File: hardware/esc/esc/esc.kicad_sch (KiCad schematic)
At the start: 9 parts, among them IC1 XMC1100T016F0016ABXUMA1, IC2 STDRIVE101TR, Q1 BSC030P03NS3G, Q2 BSC030P03NS3G, Q3 BSC030P03NS3G, Q4 BSC030P03NS3G, Q5 BSC030P03NS3G, Q6 BSC030P03NS3G, U1 AP62300Z6

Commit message: hardware edits mainly
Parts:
- removed IC1: XMC1100T016F0016ABXUMA1, SOP65P640X120-16N, symbol XMC1100T016F0016ABXUMA1:XMC1100T016F0016ABXUMA1
- removed IC2: STDRIVE101TR, QFN50P400X400X100-25N-D, symbol STDRIVE101TR:STDRIVE101TR
- removed Q1, Q2, Q3, Q4, Q5, Q6: BSC030P03NS3G, BSC0902NSATMA1, symbol BSC030N03LSGATMA1:BSC030P03NS3G
- removed U1: AP62300Z6, Package_TO_SOT_SMD:SOT-563, symbol Regulator_Switching:AP62300Z6
- added C1, C10, C11, C16, C17, C18, C23, C24, C25, C3, C30, C31, C32, C39, C40, C41, C43, C44, C45, C46, C48, C5, C50, C51, C54, C55, C57, C58, C60, C61, C63, C64, C66, C67, C71, C72, C73, C74, C75, C76, C84, C85, C88, C9, C91: 4.7uF, Capacitor_SMD:CP_Elec_6.3x7.7, symbol Device:C_Small
- added C12, C13, C14, C19, C2, C20, C21, C26, C27, C28, C33, C34, C35, C36, C37, C38, C4, C52, C53, C56, C59, C6, C62, C65, C83, C86, C89, C92: 220nF, Capacitor_SMD:C_0402_1005Metric, symbol Device:C_Small
- added C15, C22, C29, C42, C7, C8: 1nF, Capacitor_SMD:C_0603_1608Metric, symbol Device:C_Small
- added C47, C49: 18pF, Capacitor_SMD:C_0402_1005Metric, symbol Device:C_Small
- added C68: 1uF, Capacitor_SMD:C_0603_1608Metric, symbol Device:C_Small
- added C69, C70, C77, C78, C79, C80, C81, C82, C87, C90, C93: 0.1uF, Capacitor_SMD:C_0603_1608Metric, symbol Device:C_Small
- added D1, D10, D11, D12, D13, D14, D15, D16, D17, D18, D19, D2, D3, D4, D5, D6, D7, D8, D9: D_Small, Diode_SMD:D_SMA, symbol Device:D_Small
- added IC1, IC2, IC3, IC4, IC5, IC6: IR2136SPBF, SOIC127P1032X265-28N, symbol IR2136SPBF:IR2136SPBF
- added IC7: TLA2528IRTER, Package_DFN_QFN:WQFN-16-1EP_3x3mm_P0.5mm_EP1.68x1.68mm_ThermalVias, symbol TLA2528IRTER:TLA2528IRTER
- added IC8: MP9486AGN-Z, Package_SO:SOIC-8-1EP_3.9x4.9mm_P1.27mm_EP2.62x3.51mm_ThermalVias, symbol MP9486AGN-Z:MP9486AGN-Z
- added J1: USB-C, Connector_PinHeader_2.54mm:PinHeader_1x04_P2.54mm_Vertical, symbol Connector:Conn_01x04_Pin
- added J10: GPIO, Connector_PinHeader_2.54mm:PinHeader_1x04_P2.54mm_Vertical, symbol Connector:Conn_01x04_Pin
- added J11: Conn_01x08_Pin, Connector_PinHeader_1.27mm:PinHeader_1x08_P1.27mm_Vertical, symbol Connector:Conn_01x08_Pin
- added J2: DEBUG, Connector_PinHeader_2.54mm:PinHeader_1x04_P2.54mm_Vertical, symbol Connector:Conn_01x04_Pin
- added J3: TEMP-GPIO, Connector_PinHeader_1.27mm:PinHeader_1x08_P1.27mm_Vertical, symbol Connector:Conn_01x08_Pin
- added L1: 3.3uH, Inductor_SMD:L_0805_2012Metric_Pad1.05x1.20mm_HandSolder, symbol Device:L_Small
- added L2: 33uH, Inductor_SMD:L_0805_2012Metric, symbol Device:L_Small
- added Q1, Q10, Q11, Q12, Q13, Q14, Q15, Q16, Q17, Q18, Q19, Q2, Q20, Q21, Q22, Q23, Q24, Q25, Q26, Q27, Q28, Q29, Q3, Q30, Q31, Q32, Q33, Q34, Q35, Q36, Q4, Q5, Q6, Q7, Q8, Q9: NMOS, Package_SO:PowerPAK_SO-8L_Single, symbol Simulation_SPICE:NMOS
- added R1, R2, R22, R23, R24, R25, R26, R27, R3, R34, R35, R36, R37, R38, R39, R4, R46, R47, R48, R49, R5, R50, R51, R58, R59, R6, R60, R61, R62, R63, R79, R80, R81, R82, R83, R84: 10, Resistor_SMD:R_1206_3216Metric, symbol Device:R_Small
- added R10, R11, R12, R13, R14, R15, R19, R20, R21, R31, R32, R33, R43, R44, R45, R55, R56, R57, R64, R65, R66, R67, R68, R69, R70, R71, R72, R73, R74, R75, R76, R77, R78: SHUNT, Fuse:Fuse_1206_3216Metric_Pad1.42x1.75mm_HandSolder, symbol Device:R_Small
- added R16, R17, R18, R28, R29, R30, R40, R41, R42, R52, R53, R54, R7, R8, R88, R89, R9, R90: 4.7, Resistor_SMD:R_0805_2012Metric, symbol Device:R_Small
- added R91, R92: 27, Resistor_SMD:R_0402_1005Metric, symbol Device:R_Small
- added R93, R94: 1k, Resistor_SMD:R_0201_0603Metric, symbol Device:R_Small
- added R95: 33, Resistor_SMD:R_1206_3216Metric, symbol Device:R_Small
- added R96: 240k, Resistor_SMD:R_0402_1005Metric, symbol Device:R_Small
- added R97, R98: 10k, Resistor_SMD:R_0402_1005Metric, symbol Device:R_Small
- added SW1, SW2: SW_Push, Connector_PinHeader_2.54mm:PinHeader_1x02_P2.54mm_Vertical, symbol Switch:SW_Push
- added TP1, TP10, TP11, TP12, TP13, TP14, TP15, TP16, TP17, TP18, TP2, TP3, TP4, TP5, TP6, TP7, TP8, TP9: TestPoint_Small, TestPoint:TestPoint_Pad_4.0x4.0mm, symbol Connector:TestPoint_Small
- added TP19, TP20, TP21, TP22: TestPoint, TestPoint:TestPoint_Pad_4.0x4.0mm, symbol Connector:TestPoint
- added U1: RP2354B, Package_DFN_QFN:QFN-80-1EP_10x10mm_P0.4mm_EP3.4x3.4mm, symbol MCU_RaspberryPi:RP2354B
- added U10, U11, U12, U2, U3, U4, U5, U6, U7, U8, U9: INA240A2PW, Package_SO:TSSOP-8_4.4x3mm_P0.65mm, symbol Amplifier_Current:INA240A2PW
- added U14, U15: TMP110D, Package_SON:Texas_X2SON-5_0.8x0.8mm_P0.48mm, symbol Sensor_Temperature:TMP110D
- added U16: AZ1117CH2-3.3, Package_TO_SOT_SMD:SOT-223-3_TabPin2, symbol Regulator_Linear:AZ1117CH2-3.3
- added Y1: 12MHz, Crystal:Crystal_SMD_ECS_CSM3X-2Pin_7.6x4.1mm, symbol Device:Crystal
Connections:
- new net: C49.2, U1.30 (XIN), Y1.2
- new net: C16.1, C19.1, IC3.22 (VS2), Q15.1 (S), Q15.2 (S), Q15.3 (S), Q16.5 (D), TP8.1
- new net: C16.2, C19.2, IC3.24 (VB2), R29.1
- new net: Q10.1 (S), Q10.2 (S), Q10.3 (S), Q12.1 (S), Q12.2 (S), Q12.3 (S), Q8.1 (S), Q8.2 (S), Q8.3 (S), R19.2, R20.2, R21.2, U4.2 (+)
- new net: J1.2 (Pin_2), R91.2
- new net: J1.3 (Pin_3), R92.1
- new net: C11.2, C14.2, IC2.20 (VB3), R18.1
- new net: D5.1 (K), R18.2
- new net: Q4.1 (S), Q4.2 (S), Q4.3 (S), Q5.1 (S), Q5.2 (S), Q5.3 (S), Q6.1 (S), Q6.2 (S), Q6.3 (S), R10.2, R11.2, R12.2, U2.2 (+)
- new net: Q4.4 (G), R4.2
- new net: C5.2, C6.1, IC1.18 (VS3), Q1.1 (S), Q1.2 (S), Q1.3 (S), Q4.5 (D), TP6.1
- new net: C30.1, C33.1, IC5.22 (VS2), Q27.1 (S), Q27.2 (S), Q27.3 (S), Q28.5 (D), TP18.1
- new net: C30.2, C33.2, IC5.24 (VB2), R53.1
- new net: C32.2, C35.2, IC5.20 (VB3), R54.1
- new net: D14.1 (K), R54.2
- new net: C17.1, C20.1, IC3.28 (VB1), R28.1
- new net: C17.2, C20.2, IC3.26 (VS1), Q17.1 (S), Q17.2 (S), Q17.3 (S), Q18.5 (D), TP7.1
- new net: Q35.1 (S), Q35.2 (S), Q35.3 (S), R76.2, R77.2, R78.2, U12.2 (+)
- new net: Q35.4 (G), R84.2
- new net: C36.1, C39.1, IC6.18 (VS3), Q35.5 (D), Q36.1 (S), Q36.2 (S), Q36.3 (S), TP15.1
- new net: IC1.23 (HO2), R2.1
- new net: Q2.4 (G), R2.2
- new net: IC2.15 (LO2), R24.1
- new net: Q10.4 (G), R24.2
- new net: Q28.1 (S), Q28.2 (S), Q28.3 (S), R67.2, R68.2, R69.2, U8.2 (+)
- new net: Q28.4 (G), R60.2
- new net: Q20.1 (S), Q20.2 (S), Q20.3 (S), Q22.1 (S), Q22.2 (S), Q22.3 (S), Q24.1 (S), Q24.2 (S), Q24.3 (S), R43.2, R44.2, R45.2, U6.2 (+)
- new net: C47.2, U1.31 (XOUT), Y1.1
- new net: C29.1, IC5.11 (RCIN)
- new net: R93.2, SW1.1, SW2.1, U1.35 (RUN)
- new net: R94.1, SW2.2
- new net: Q36.4 (G), R83.2
- new net: IC2.23 (HO2), R26.1
- new net: Q9.4 (G), R26.2
- new net: D15.1 (K), R53.2
- new net: C22.1, IC4.11 (RCIN)
- new net: C23.1, C26.1, IC4.22 (VS2), Q21.1 (S), Q21.2 (S), Q21.3 (S), Q22.5 (D), TP11.1
- new net: C23.2, C26.2, IC4.24 (VB2), R41.1
- new net: Q17.4 (G), R39.2
- new net: C31.1, C34.1, IC5.28 (VB1), R52.1
- new net: C31.2, C34.2, IC5.26 (VS1), Q29.1 (S), Q29.2 (S), Q29.3 (S), Q30.5 (D), TP17.1
- new net: C10.2, C13.2, IC2.26 (VS1), Q11.1 (S), Q11.2 (S), Q11.3 (S), Q12.5 (D), TP1.1
- new net: Q31.1 (S), Q31.2 (S), Q31.3 (S), R13.2, R14.2, R15.2, U10.2 (+)
- new net: C25.1, C28.1, IC4.18 (VS3), Q19.1 (S), Q19.2 (S), Q19.3 (S), Q20.5 (D), TP12.1
- new net: Q19.4 (G), R47.2
- new net: IC3.27 (HO1), R39.1
- new net: C12.2, C9.1, IC2.24 (VB2), R17.1
- new net: D6.1 (K), R17.2
- new net: IC5.19 (HO3), R59.1
- new net: Q25.4 (G), R59.2
- new net: Q14.1 (S), Q14.2 (S), Q14.3 (S), Q16.1 (S), Q16.2 (S), Q16.3 (S), Q18.1 (S), Q18.2 (S), Q18.3 (S), R31.2, R32.2, R33.2, U5.2 (+)
- new net: Q18.4 (G), R37.2
- new net: IC7.13 (SCL), U1.12 (GPIO13), U14.2 (SCL), U15.2 (SCL)
- new net: U1.13 (GPIO14), U14.3 (ADD0)
- new net: IC7.14 (SDA), U1.11 (GPIO12), U14.4 (SDA), U15.4 (SDA)
- new net: Q5.4 (G), R5.2
- new net: C3.2, C4.1, IC1.22 (VS2), Q2.1 (S), Q2.2 (S), Q2.3 (S), Q5.5 (D), TP5.1
- new net: C24.2, C27.2, IC4.26 (VS1), Q23.1 (S), Q23.2 (S), Q23.3 (S), Q24.5 (D), TP10.1
- new net: C25.2, C28.2, IC4.20 (VB3), R42.1
- new net: D11.1 (K), R42.2
- new net: C18.1, C21.1, IC3.18 (VS3), Q13.1 (S), Q13.2 (S), Q13.3 (S), Q14.5 (D), TP9.1
- new net: C18.2, C21.2, IC3.20 (VB3), R30.1
- new net: C36.2, C39.2, IC6.20 (VB3), R88.1
- new net: C37.2, C40.2, IC6.26 (VS1), Q31.5 (D), Q32.1 (S), Q32.2 (S), Q32.3 (S), TP13.1
- new net: D9.1 (K), R29.2
- new net: D3.1 (K), R9.2
- new net: Q8.4 (G), R22.2
- new net: C11.1, C14.1, IC2.18 (VS3), Q7.1 (S), Q7.2 (S), Q7.3 (S), Q8.5 (D), TP3.1
- new net: Q33.1 (S), Q33.2 (S), Q33.3 (S), R73.2, R74.2, R75.2, U11.2 (+)
- new net: R55.2, R56.2, R57.2, R64.1, R65.1, R66.1, R67.1, R68.1, R69.1, R70.1, R71.1, R72.1, U7.2 (+)
- new net: Q30.1 (S), Q30.2 (S), Q30.3 (S), R64.2, R65.2, R66.2, U3.2 (+)
- new net: Q6.4 (G), R6.2
- new net: C1.2, C2.2, IC1.26 (VS1), Q3.1 (S), Q3.2 (S), Q3.3 (S), Q6.5 (D), TP4.1
- new net: C1.1, C2.1, IC1.28 (VB1), R8.1
- new net: R93.1, U1.75 (~{QSPI_SS})
- new net: Q29.4 (G), R63.2
- new net: D18.1 (K), R90.2
- new net: C38.1, C41.1, IC6.22 (VS2), Q33.5 (D), Q34.1 (S), Q34.2 (S), Q34.3 (S), TP14.1
- new net: Q34.4 (G), R80.2
- new net: IC8.6 (DIM), IC8.7 (EN), R98.1
- new net: Q26.1 (S), Q26.2 (S), Q26.3 (S), R70.2, R71.2, R72.2, U9.2 (+)
- new net: IC4.23 (HO2), R50.1
- new net: Q21.4 (G), R50.2
- new net: C38.2, C41.2, IC6.24 (VB2), R89.1
- new net: C42.1, IC6.11 (RCIN)
- new net: Q22.4 (G), R48.2
- new net: IC6.15 (LO2), R82.1
- new net: Q33.4 (G), R82.2
- new net: D1.1 (K), R8.2
- new net: D12.1 (K), R41.2
- new net: C44.1, R95.1, U1.61 (VREG_AVDD)
- new net: IC5.14 (LO3), R61.1
- new net: Q30.4 (G), R61.2
- new net: IC4.16 (LO1), R46.1
- new net: Q20.4 (G), R46.2
- new net: Q26.4 (G), R58.2
- new net: C32.1, C35.1, IC5.18 (VS3), Q25.1 (S), Q25.2 (S), Q25.3 (S), Q26.5 (D), TP16.1
- new net: C77.1, U16.2 (GND)
- new net: IC4.15 (LO2), R48.1
- new net: IC7.15 (AIN0/GPIO0), J3.1 (Pin_1)
- new net: IC7.16 (AIN1/GPIO1), J3.2 (Pin_2)
- new net: IC7.1 (AIN2/GPIO2), J3.3 (Pin_3)
- new net: IC7.2 (AIN3/GPIO3), J3.4 (Pin_4)
- new net: IC7.3 (AIN4/GPIO4), J3.5 (Pin_5)
- new net: IC7.4 (AIN5/GPIO5), J3.6 (Pin_6)
- new net: IC7.5 (AIN6/GPIO6), J3.7 (Pin_7)
- new net: IC7.6 (AIN7/GPIO7), J3.8 (Pin_8)
- new net: IC2.14 (LO3), R25.1
- new net: Q12.4 (G), R25.2
- new net: IC1.9 (ITRIP), U1.4 (GPIO7), U2.8
- new net: U1.54 (GPIO43/ADC3), U10.8
- new net: Q31.4 (G), R81.2
- new net: D4.1 (K), R16.2
- new net: C10.1, C13.1, IC2.28 (VB1), R16.1
- new net: IC3.10 (EN), U1.44 (GPIO35)
- new net: C15.1, IC3.11 (RCIN)
- new net: IC3.14 (LO3), R37.1
- new net: IC3.15 (LO2), R36.1
- new net: IC3.16 (LO1), R34.1
- new net: IC3.19 (HO3), R35.1
- new net: IC3.2 (~{HIN1}), IC4.2 (~{HIN1}), IC5.2 (~{HIN1}), U1.38 (GPIO30)
- new net: IC3.23 (HO2), R38.1
- new net: IC3.3 (~{HIN2}), IC4.3 (~{HIN2}), IC5.3 (~{HIN2}), U1.40 (GPIO32)
- new net: IC3.4 (~{HIN3}), IC4.4 (~{HIN3}), IC5.4 (~{HIN3}), U1.43 (GPIO34)
- new net: IC3.5 (~{LIN1}), IC4.5 (~{LIN1}), IC5.5 (~{LIN1}), U1.45 (GPIO36)
- new net: IC3.6 (~{LIN2}), IC4.6 (~{LIN2}), IC5.6 (~{LIN2}), U1.47 (GPIO38)
- new net: IC3.7 (~{LIN3}), IC4.7 (~{LIN3}), IC5.7 (~{LIN3}), U1.48 (GPIO39)
- new net: IC3.8 (~{FAULT}), U1.46 (GPIO37)
- new net: IC3.9 (ITRIP), U1.26 (GPIO25), U5.8
- new net: IC1.14 (LO3), R6.1
- new net: C70.2, IC8.1 (FB), R96.1, R97.2
- new net: Q1.4 (G), R3.2
- new net: C24.1, C27.1, IC4.28 (VB1), R40.1
- new net: Q14.4 (G), R34.2
- new net: C37.1, C40.1, IC6.28 (VB1), R90.1
- new net: D13.1 (K), R52.2
- new net: Q32.4 (G), R79.2
- new net: C68.1, IC7.8 (DECAP)
- new net: IC6.23 (HO2), R80.1
- new net: Q3.4 (G), R1.2
- new net: IC2.10 (EN), U1.9 (GPIO11)
- new net: C8.1, IC2.11 (RCIN)
- new net: IC2.16 (LO1), R22.1
- new net: IC2.19 (HO3), R23.1
- new net: IC1.2 (~{HIN1}), IC2.2 (~{HIN1}), IC6.2 (~{HIN1}), U1.77 (GPIO0)
- new net: C12.1, C9.2, IC2.22 (VS2), Q10.5 (D), Q9.1 (S), Q9.2 (S), Q9.3 (S), TP2.1
- new net: IC2.27 (HO1), R27.1
- new net: IC1.3 (~{HIN2}), IC2.3 (~{HIN2}), IC6.3 (~{HIN2}), U1.79 (GPIO2)
- new net: IC1.4 (~{HIN3}), IC2.4 (~{HIN3}), IC6.4 (~{HIN3}), U1.1 (GPIO4)
- new net: IC1.5 (~{LIN1}), IC2.5 (~{LIN1}), IC6.5 (~{LIN1}), U1.3 (GPIO6)
- new net: IC1.6 (~{LIN2}), IC2.6 (~{LIN2}), IC6.6 (~{LIN2}), U1.6 (GPIO8)
- new net: IC1.7 (~{LIN3}), IC2.7 (~{LIN3}), IC6.7 (~{LIN3}), U1.8 (GPIO10)
- new net: IC2.8 (~{FAULT}), U1.7 (GPIO9)
- new net: IC2.9 (ITRIP), U1.58 (GPIO47/ADC7), U4.8
- new net: D16.1 (K), R89.2
- new net: L1.2, U1.63 (VREG_LX)
- new net: C5.1, C6.2, IC1.20 (VB3), R9.1
- new net: IC4.14 (LO3), R49.1
- new net: Q24.4 (G), R49.2
- new net: IC1.15 (LO2), R5.1
- new net: D17.1 (K), R88.2
- new net: U1.14 (GPIO15), U15.3 (ADD0)
- new net: IC7.11 (ADDR), U1.2 (GPIO5)
- new net: C69.1, D19.1 (K), IC8.5 (SW), L2.2
- new net: C69.2, IC8.4 (BST)
- new net: C3.1, C4.2, IC1.24 (VB2), R7.1
- new net: IC1.19 (HO3), R3.1
- new net: D2.1 (K), R7.2
- new net: IC6.16 (LO1), R84.1
- new net: D10.1 (K), R40.2
- new net: U1.56 (GPIO45/ADC5), U12.8
- new net: Q27.4 (G), R62.2
- new net: IC5.9 (ITRIP), U7.8
- new net: IC6.27 (HO1), R79.1
- new net: IC1.16 (LO1), R4.1
- new net: IC4.27 (HO1), R51.1
- new net: Q23.4 (G), R51.2
- new net: Q16.4 (G), R36.2
- new net: U1.53 (GPIO42/ADC2), U9.8
- new net: Q13.4 (G), R35.2
- new net: IC1.27 (HO1), R1.1
- new net: Q11.4 (G), R27.2
- new net: IC5.27 (HO1), R63.1
- new net: R92.2, U1.67 (USB_DP)
- new net: J11.3 (Pin_3), U1.25 (GPIO24)
- new net: J11.4 (Pin_4), U1.23 (GPIO23)
- new net: J11.5 (Pin_5), U1.22 (GPIO22)
- new net: J11.6 (Pin_6), U1.21 (GPIO21)
- new net: IC4.9 (ITRIP), U1.57 (GPIO46/ADC6), U6.8
- new net: J2.3 (Pin_3), U1.33 (SWCLK)
- new net: J2.4 (Pin_4), U1.34 (SWDIO)
- new net: J10.1 (Pin_1), U1.19 (GPIO19)
- new net: J10.2 (Pin_2), U1.18 (GPIO18)
- new net: J10.3 (Pin_3), U1.17 (GPIO17)
- new net: J10.4 (Pin_4), U1.16 (GPIO16)
- new net: IC4.19 (HO3), R47.1
- new net: IC1.10 (EN), U1.80 (GPIO3)
- new net: C7.1, IC1.11 (RCIN)
- new net: IC1.8 (~{FAULT}), U1.78 (GPIO1)
- new net: IC5.10 (EN), U1.36 (GPIO28)
- new net: IC5.15 (LO2), R60.1
- new net: IC5.16 (LO1), R58.1
- new net: IC5.23 (HO2), R62.1
- new net: IC5.8 (~{FAULT}), U1.37 (GPIO29)
- new net: D7.1 (K), R28.2
- new net: D8.1 (K), R30.2
- new net: Q15.4 (G), R38.2
- new net: R91.1, U1.66 (USB_DM)
- new net: IC4.10 (EN), U1.39 (GPIO31)
- new net: IC4.8 (~{FAULT}), U1.42 (GPIO33)
- new net: IC6.8 (~{FAULT}), U1.27 (GPIO26)
- new net: IC6.10 (EN), U1.28 (GPIO27)
- new net: U1.49 (GPIO40/ADC0), U3.8
- new net: U1.52 (GPIO41/ADC1), U8.8
- new net: U1.55 (GPIO44/ADC4), U11.8
- new net: Q7.4 (G), R23.2
- new net: IC6.14 (LO3), R81.1
- new net: IC6.19 (HO3), R83.1
- new net +1V1: C43.2, C46.2, J2.1 (Pin_1), L1.1, U1.10 (DVDD), U1.32 (DVDD), U1.51 (DVDD), U1.65 (VREG_FB)
- new net +3V3: C45.1, C48.2, C50.1, C51.1, C52.1, C53.1, C54.1, C55.1, C56.1, C57.1, C58.1, C59.1, C60.1, C61.1, C62.1, C63.1, C64.1, C65.1, C66.1, C67.1, C77.2, C78.2, C79.2, C80.2, C81.2, D1.2 (A), D10.2 (A), D11.2 (A), D12.2 (A), D13.2 (A), D14.2 (A), D15.2 (A), D16.2 (A), D17.2 (A), D18.2 (A), D2.2 (A), D3.2 (A), D4.2 (A), D5.2 (A), D6.2 (A), D7.2 (A), D8.2 (A), D9.2 (A), IC1.1 (VCC), IC2.1 (VCC), IC3.1 (VCC), IC4.1 (VCC), IC5.1 (VCC), IC6.1 (VCC), IC7.10 (DVDD), IC7.7 (AVDD), J2.2 (Pin_2), R95.2, U1.15 (IOVDD), U1.24 (IOVDD), U1.29 (IOVDD), U1.41 (IOVDD), U1.5 (IOVDD), U1.50 (IOVDD), U1.59 (ADC_AVDD), U1.60 (IOVDD), U1.64 (VREG_VIN), U1.69 (QSPI_IOVDD), U1.76 (IOVDD), U10.5 (V+), U10.6 (REF2), U11.5 (V+), U11.6 (REF2), U12.5 (V+), U12.6 (REF2), U14.5 (V+), U15.5 (V+), U16.3 (OUT), U2.5 (V+), U2.6 (REF2), U3.5 (V+), U3.6 (REF2), U4.5 (V+), U4.6 (REF2), U5.5 (V+), U5.6 (REF2), U6.5 (V+), U6.6 (REF2), U7.5 (V+), U7.6 (REF2), U8.5 (V+), U8.6 (REF2), U9.5 (V+), U9.6 (REF2)
- new net +5V: C70.1, C71.1, C72.1, C73.1, C74.1, C75.1, C76.1, C82.2, C83.1, C84.1, C85.1, C86.1, C87.2, C88.2, C89.2, C90.1, C91.2, C92.2, C93.1, J1.4 (Pin_4), J11.2 (Pin_2), L2.1, R96.2, U16.1 (IN)
- new net +BATT: IC8.3 (VIN), J11.7 (Pin_7), Q1.5 (D), Q11.5 (D), Q13.5 (D), Q15.5 (D), Q17.5 (D), Q19.5 (D), Q2.5 (D), Q21.5 (D), Q23.5 (D), Q25.5 (D), Q27.5 (D), Q29.5 (D), Q3.5 (D), Q32.5 (D), Q34.5 (D), Q36.5 (D), Q7.5 (D), Q9.5 (D), R98.2, TP20.1, TP21.1
- new net GND: C15.2, C22.2, C29.2, C42.2, C43.1, C44.2, C45.2, C46.1, C47.1, C48.1, C49.1, C50.2, C51.2, C52.2, C53.2, C54.2, C55.2, C56.2, C57.2, C58.2, C59.2, C60.2, C61.2, C62.2, C63.2, C64.2, C65.2, C66.2, C67.2, C68.2, C7.2, C71.2, C72.2, C73.2, C74.2, C75.2, C76.2, C78.1, C79.1, C8.2, C80.1, C81.1, C82.1, C83.2, C84.2, C85.2, C86.2, C87.1, C88.1, C89.1, C90.2, C91.1, C92.1, C93.2, D19.2 (A), IC1.12 (VSS), IC1.13 (COM), IC1.17 (NC_1), IC1.21 (NC_2), IC1.25 (NC_3), IC2.12 (VSS), IC2.13 (COM), IC2.17 (NC_1), IC2.21 (NC_2), IC2.25 (NC_3), IC3.12 (VSS), IC3.13 (COM), IC3.17 (NC_1), IC3.21 (NC_2), IC3.25 (NC_3), IC4.12 (VSS), IC4.13 (COM), IC4.17 (NC_1), IC4.21 (NC_2), IC4.25 (NC_3), IC5.12 (VSS), IC5.13 (COM), IC5.17 (NC_1), IC5.21 (NC_2), IC5.25 (NC_3), IC6.12 (VSS), IC6.13 (COM), IC6.17 (NC_1), IC6.21 (NC_2), IC6.25 (NC_3), IC7.17 (EP), IC7.9 (GND), IC8.8 (GND), IC8.9 (EP), J1.1 (Pin_1), J11.1 (Pin_1), J11.8 (Pin_8), R10.1, R11.1, R12.1, R13.1, R14.1, R15.1, R19.1, R20.1, R21.1, R31.1, R32.1, R33.1, R43.1, R44.1, R45.1, R55.1, R56.1, R57.1, R73.1, R74.1, R75.1, R76.1, R77.1, R78.1, R94.2, R97.1, SW1.2, TP19.1, TP22.1, U1.62 (VREG_PGND), U1.81 (GND), U10.1 (GND), U10.3 (-), U10.4 (GND), U10.7 (REF1), U11.1 (GND), U11.3 (-), U11.4 (GND), U11.7 (REF1), U12.1 (GND), U12.3 (-), U12.4 (GND), U12.7 (REF1), U14.1 (GND), U15.1 (GND), U2.1 (GND), U2.3 (-), U2.4 (GND), U2.7 (REF1), U3.1 (GND), U3.3 (-), U3.4 (GND), U3.7 (REF1), U4.1 (GND), U4.3 (-), U4.4 (GND), U4.7 (REF1), U5.1 (GND), U5.3 (-), U5.4 (GND), U5.7 (REF1), U6.1 (GND), U6.3 (-), U6.4 (GND), U6.7 (REF1), U7.1 (GND), U7.3 (-), U7.4 (GND), U7.7 (REF1), U8.1 (GND), U8.3 (-), U8.4 (GND), U8.7 (REF1), U9.1 (GND), U9.3 (-), U9.4 (GND), U9.7 (REF1)

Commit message: block 1x1
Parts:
- removed R55, R56, R57: SHUNT, Fuse:Fuse_1206_3216Metric_Pad1.42x1.75mm_HandSolder, symbol Device:R_Small
- removed U7: INA240A2PW, Package_SO:TSSOP-8_4.4x3mm_P0.65mm, symbol Amplifier_Current:INA240A2PW
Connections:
- net GND: now also R64.1, R65.1, R66.1, R67.1, R68.1, R69.1, R70.1, R71.1, R72.1

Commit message: block 2z1
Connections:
- net at C37.2, IC6.26 (VS1), Q31.5 (D)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: now also C40.1; no longer C40.2
- net at C37.1, IC6.28 (VB1), R90.1: now also C40.2; no longer C40.1
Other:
- moved on the sheet: C40
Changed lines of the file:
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@@
 	)
 	(junction
-		(at 478.79 44.45)
-		(diameter 0)
-		(color 0 0 0 0)
-	)
-	(junction
 		(at 242.57 186.69)
 		(diameter 0)
@@
 	)
 	(junction
+		(at 480.06 39.37)
+		(diameter 0)
+		(color 0 0 0 0)
+	)
+	(junction
 		(at 270.51 41.91)
 		(diameter 0)
@@
 	)
 	(junction
+		(at 480.06 44.45)
+		(diameter 0)
+		(color 0 0 0 0)
+	)
+	(junction
 		(at 185.42 175.26)
 		(diameter 0)
@@
 	)
 	(junction
-		(at 478.79 39.37)
-		(diameter 0)
-		(color 0 0 0 0)
-	)
-	(junction
 		(at 276.86 58.42)
 		(diameter 0)
@@
 	(wire
 		(pts
-			(xy 463.55 39.37) (xy 478.79 39.37)
+			(xy 463.55 39.37) (xy 480.06 39.37)
 		)
 		(stroke
@@
 	(wire
 		(pts
-			(xy 478.79 39.37) (xy 490.22 39.37)
+			(xy 480.06 39.37) (xy 490.22 39.37)
 		)
 		(stroke
@@
 	(wire
 		(pts
-			(xy 478.79 44.45) (xy 490.22 44.45)
-		)
-		(stroke
-			(width 0)
-			(type default)
-		)
-	)
-	(wire
-		(pts
 			(xy 443.23 382.27) (xy 429.26 382.27)
 		)
@@
 	(wire
 		(pts
-			(xy 468.63 44.45) (xy 478.79 44.45)
+			(xy 468.63 44.45) (xy 480.06 44.45)
 		)
 		(stroke
@@
 	(wire
 		(pts
+			(xy 480.06 44.45) (xy 490.22 44.45)
+		)
+		(stroke
+			(width 0)
+			(type default)
+		)
+	)
+	(wire
+		(pts
 			(xy 24.13 127) (xy 29.21 127)
 		)
@@
 	(symbol
 		(lib_id "Device:C_Small")
-		(at 478.79 41.91 0)
+		(at 480.06 41.91 180)
 		(unit 1)
 		(exclude_from_sim no)
@@
 		(fields_autoplaced yes)
 		(property "Reference" "C40"
-			(at 481.33 40.6462 0)
+			(at 482.6 40.6335 0)
 			(effects
 				(font
 					(size 1.27 1.27)
 				)
-				(justify left)
+				(justify right)
 			)
 		)
 		(property "Value" "4.7uF"
-			(at 481.33 43.1862 0)
+			(at 482.6 43.1735 0)
 			(effects
 				(font
 					(size 1.27 1.27)
 				)
-				(justify left)
+				(justify right)
 			)
 		)
 		(property "Footprint" "Capacitor_SMD:CP_Elec_6.3x7.7"
-			(at 478.79 41.91 0)
+			(at 480.06 41.91 0)
 			(effects
 				(font
@@
 		)
 		(property "Datasheet" "~"
-			(at 478.79 41.91 0)
+			(at 480.06 41.91 0)
 			(effects
 				(font
@@
 		)
 		(property "Description" "Unpolarized capacitor, small symbol"
-			(at 478.79 41.91 0)
+			(at 480.06 41.91 0)
 			(effects
 				(font

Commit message: block 2x2 zoing updates
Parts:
- removed C60, C63, C66, C67, C84, C88: 4.7uF, Capacitor_SMD:CP_Elec_6.3x7.7, symbol Device:C_Small
- C50, C57: value 4.7uF -> 1uF
- C54, C55, C58: value 4.7uF -> 10uF
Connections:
- net at C20.1, IC3.28 (VB1), R28.1: now also C17.2; no longer C17.1
- net at C20.2, IC3.26 (VS1), Q17.1 (S)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: now also C17.1; no longer C17.2
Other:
- moved on the sheet: C17

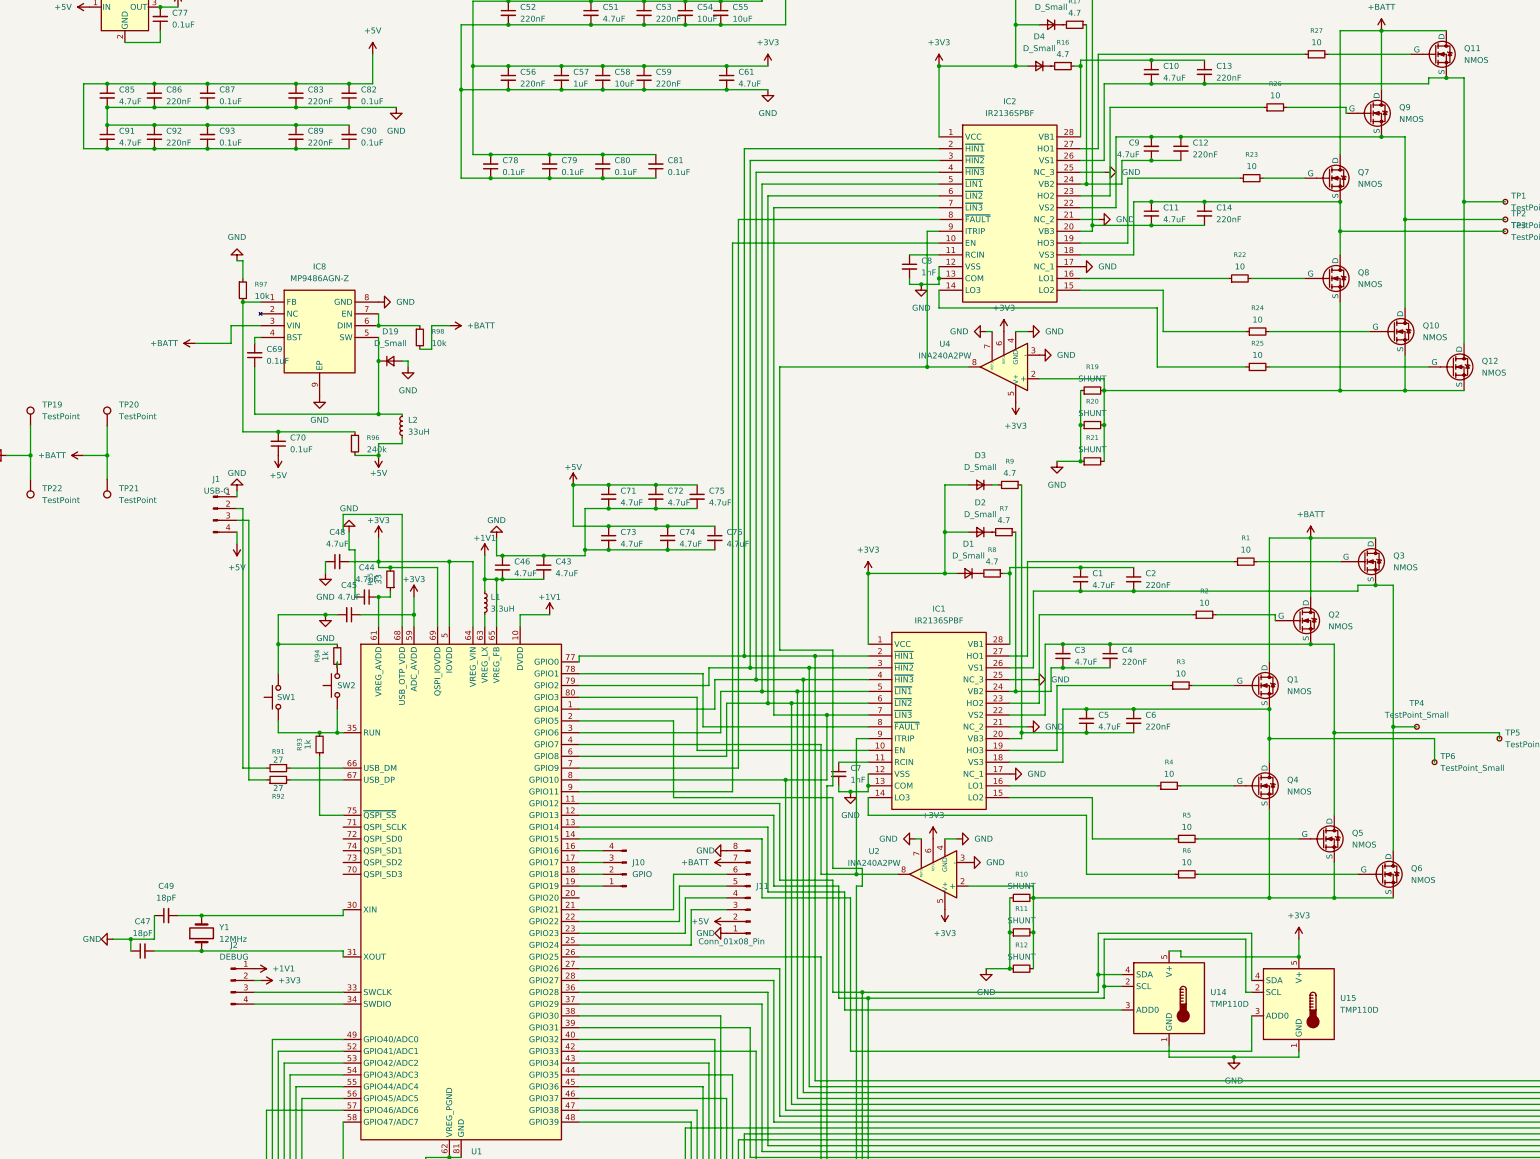
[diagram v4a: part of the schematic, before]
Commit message: row 3 zoning in place
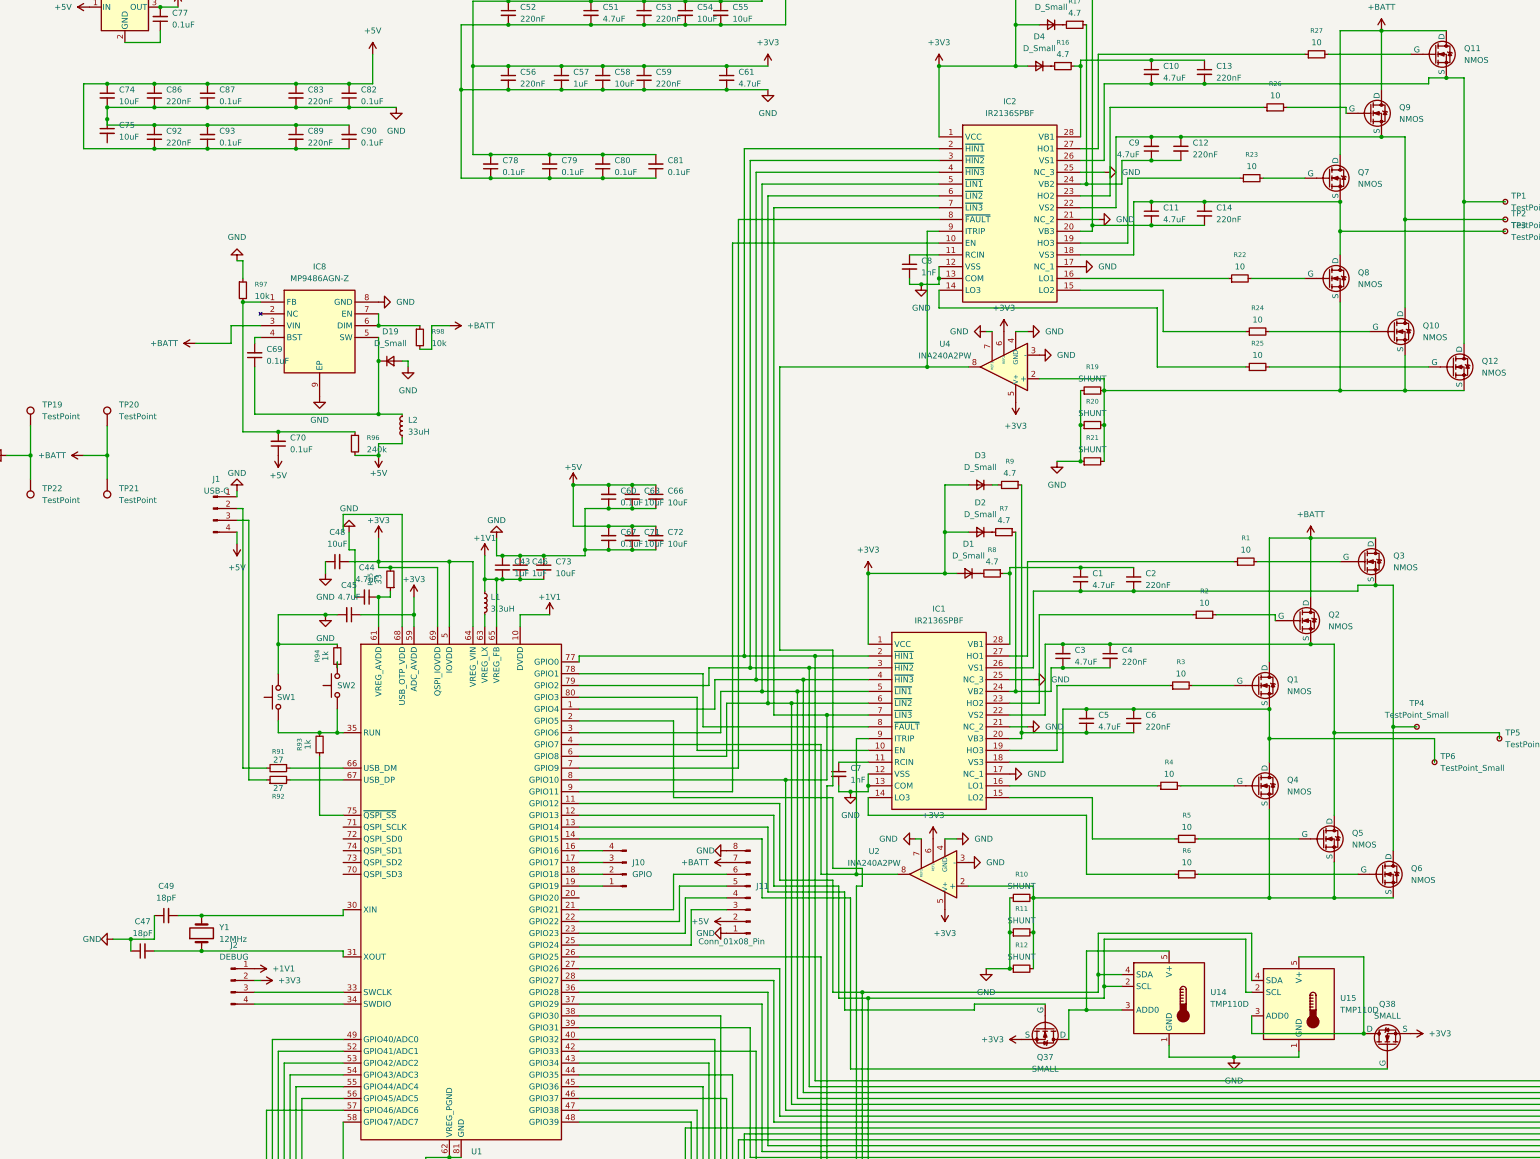
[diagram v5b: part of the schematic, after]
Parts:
- removed C76, C85, C91: 4.7uF, Capacitor_SMD:CP_Elec_6.3x7.7, symbol Device:C_Small
- added C60, C67: 0.1uF, Capacitor_SMD:C_0603_1608Metric, symbol Device:C_Small
- added C63, C66: 10uF, Capacitor_SMD:CP_Elec_6.3x7.7, symbol Device:C_Small
- added Q37, Q38: SMALL, Package_TO_SOT_SMD:SOT-23-3, symbol Simulation_SPICE:NMOS
- C43, C46: value 4.7uF -> 1uF
- C48, C71, C72, C73, C74, C75: value 4.7uF -> 10uF
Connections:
- net +1V1: now also C73.2
- net +3V3: now also Q37.3 (S), Q38.3 (S); no longer U14.5 (V+), U15.5 (V+)
- net +5V: now also C60.2, C63.1, C66.1, C67.2; no longer C73.1, C75.1
- net GND: now also C73.1, C75.1, C60.1, C63.2, C66.2, C67.1; no longer C73.2, C75.2
- net at U14.3 (ADD0): now also U14.5 (V+), Q37.1 (D); no longer U1.13 (GPIO14)
- net at U15.3 (ADD0): now also U15.5 (V+), Q38.1 (D); no longer U1.14 (GPIO15)
- new net: Q38.2 (G), U1.14 (GPIO15)
- new net: Q37.2 (G), U1.13 (GPIO14)

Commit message: power elec nearly done
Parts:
- removed C75: 10uF, Capacitor_SMD:CP_Elec_6.3x7.7, symbol Device:C_Small
- added C76: 10uF, Capacitor_SMD:C_0402_1005Metric, symbol Device:C_Small
- added R55: 1k, Resistor_SMD:R_0201_0603Metric, symbol Device:R_Small
- C43, C46, C48, C50, C54, C55, C57, C58, C63, C66, C71, C72, C73, C74: footprint Capacitor_SMD:CP_Elec_6.3x7.7 -> Capacitor_SMD:C_0402_1005Metric
- C61: value 4.7uF -> 10uF; footprint Capacitor_SMD:CP_Elec_6.3x7.7 -> Capacitor_SMD:C_0402_1005Metric
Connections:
- net +5V: now also C76.2
- net GND: now also C77.1, U16.2 (GND), C76.1, R55.2
- net at IC8.6 (DIM), IC8.7 (EN), R98.1: now also R55.1

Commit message: signals
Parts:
- removed C51, C64: 4.7uF, Capacitor_SMD:CP_Elec_6.3x7.7, symbol Device:C_Small
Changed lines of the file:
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@@
 	)
 	(junction
-		(at 149.86 19.05)
-		(diameter 0)
-		(color 0 0 0 0)
-	)
-	(junction
 		(at 439.42 234.95)
 		(diameter 0)
@@
 	)
 	(junction
-		(at 149.86 29.21)
-		(diameter 0)
-		(color 0 0 0 0)
-	)
-	(junction
 		(at 257.81 311.15)
 		(diameter 0)
@@
 	)
 	(junction
-		(at 149.86 24.13)
-		(diameter 0)
-		(color 0 0 0 0)
-	)
-	(junction
 		(at 492.76 234.95)
 		(diameter 0)
@@
 	)
 	(junction
-		(at 149.86 34.29)
-		(diameter 0)
-		(color 0 0 0 0)
-	)
-	(junction
 		(at 238.76 341.63)
 		(diameter 0)
@@
 	(wire
 		(pts
-			(xy 161.29 34.29) (xy 149.86 34.29)
-		)
-		(stroke
-			(width 0)
-			(type default)
-		)
-	)
-	(wire
-		(pts
 			(xy 440.69 349.25) (xy 453.39 349.25)
 		)
@@
 	(wire
 		(pts
-			(xy 149.86 24.13) (xy 161.29 24.13)
+			(xy 132.08 24.13) (xy 161.29 24.13)
 		)
 		(stroke
@@
 	(wire
 		(pts
-			(xy 132.08 34.29) (xy 149.86 34.29)
+			(xy 132.08 34.29) (xy 161.29 34.29)
 		)
 		(stroke
@@
 	(wire
 		(pts
-			(xy 161.29 29.21) (xy 149.86 29.21)
-		)
-		(stroke
-			(width 0)
-			(type default)
-		)
-	)
-	(wire
-		(pts
 			(xy 85.09 293.37) (xy 85.09 260.35)
 		)
@@
 	(wire
 		(pts
-			(xy 132.08 19.05) (xy 149.86 19.05)
-		)
-		(stroke
-			(width 0)
-			(type default)
-		)
-	)
-	(wire
-		(pts
 			(xy 455.93 152.4) (xy 455.93 160.02)
 		)
@@
 	(wire
 		(pts
-			(xy 132.08 24.13) (xy 149.86 24.13)
-		)
-		(stroke
-			(width 0)
-			(type default)
-		)
-	)
-	(wire
-		(pts
 			(xy 260.35 243.84) (xy 260.35 241.3)
 		)
@@
 	(wire
 		(pts
-			(xy 132.08 29.21) (xy 149.86 29.21)
+			(xy 132.08 29.21) (xy 161.29 29.21)
 		)
 		(stroke
@@
 	(wire
 		(pts
-			(xy 149.86 19.05) (xy 161.29 19.05)
+			(xy 132.08 19.05) (xy 161.29 19.05)
 		)
 		(stroke
@@
 	)
 	(symbol
-		(lib_id "Device:C_Small")
-		(at 149.86 21.59 0)
-		(unit 1)
-		(exclude_from_sim no)
-		(in_bom yes)
-		(on_board yes)
-		(dnp no)
-		(fields_autoplaced yes)
-		(property "Reference" "C64"
-			(at 152.4 20.3262 0)
-			(effects
-				(font
-					(size 1.27 1.27)
-				)
-				(justify left)
-			)
-		)
-		(property "Value" "4.7uF"
-			(at 152.4 22.8662 0)
-			(effects
-				(font
-					(size 1.27 1.27)
-				)
-				(justify left)
-			)
-		)
-		(property "Footprint" "Capacitor_SMD:CP_Elec_6.3x7.7"
-			(at 149.86 21.59 0)
-			(effects
-				(font
-					(size 1.27 1.27)
-				)
-				(hide yes)
-			)
-		)
-		(property "Datasheet" "~"
-			(at 149.86 21.59 0)
-			(effects
-				(font
-					(size 1.27 1.27)
-				)
-				(hide yes)
-			)
-		)
-		(property "Description" "Unpolarized capacitor, small symbol"
-			(at 149.86 21.59 0)
-			(effects
-				(font
-					(size 1.27 1.27)
-				)
-				(hide yes)
-			)
-		)
-		(pin "2"
-		)
-		(pin "1"
-		)
-		(instances
-			(project "esc"
-				(path "/98640010-11bc-4686-91cc-8acbb55a5e3d"
-					(reference "C64")
-					(unit 1)
-				)
-			)
-		)
-	)
-	(symbol
 		(lib_id "Device:R_Small")
 		(at 322.58 308.61 90)
@@
 					(unit 1)
 				)
-			)
-		)
-	)
-	(symbol
-		(lib_id "Device:C_Small")
-		(at 149.86 31.75 0)
-		(unit 1)
-		(exclude_from_sim no)
-		(in_bom yes)
-		(on_board yes)
-		(dnp no)
-		(fields_autoplaced yes)
-		(property "Reference" "C51"
-			(at 152.4 30.4862 0)
-			(effects
-				(font
-					(size 1.27 1.27)
-				)
-				(justify left)
-			)
-		)
-		(property "Value" "4.7uF"
-			(at 152.4 33.0262 0)
-			(effects
-				(font
-					(size 1.27 1.27)
-				)
-				(justify left)
-			)
-		)
-		(property "Footprint" "Capacitor_SMD:CP_Elec_6.3x7.7"
-			(at 149.86 31.75 0)
-			(effects
-				(font
-					(size 1.27 1.27)
-				)
-				(hide yes)
-			)
-		)
-		(property "Datasheet" "~"
-			(at 149.86 31.75 0)
-			(effects
-				(font
-					(size 1.27 1.27)
-				)
-				(hide yes)
-			)
-		)
-		(property "Description" "Unpolarized capacitor, small symbol"
-			(at 149.86 31.75 0)
-			(effects
-				(font
-					(size 1.27 1.27)
-				)
-				(hide yes)
-			)
-		)
-		(pin "2"
-		)
-		(pin "1"
-		)
-		(instances
-			(project "esc"
-				(path "/98640010-11bc-4686-91cc-8acbb55a5e3d"
-					(reference "C51")
-					(unit 1)
-				)
